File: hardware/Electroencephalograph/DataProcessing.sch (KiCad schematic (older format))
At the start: 20 parts, among them J3 Conn_01x04_Female, J4 Conn_01x04_Female, U3 STM32F030K6Tx, Y1 20MHz

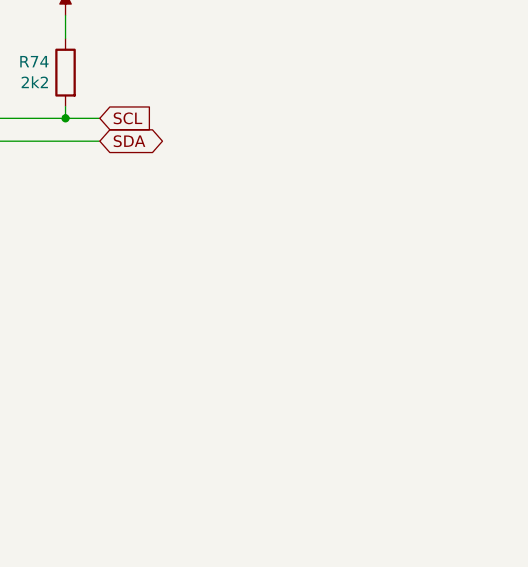
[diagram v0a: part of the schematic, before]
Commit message: split user interface to separate sheets
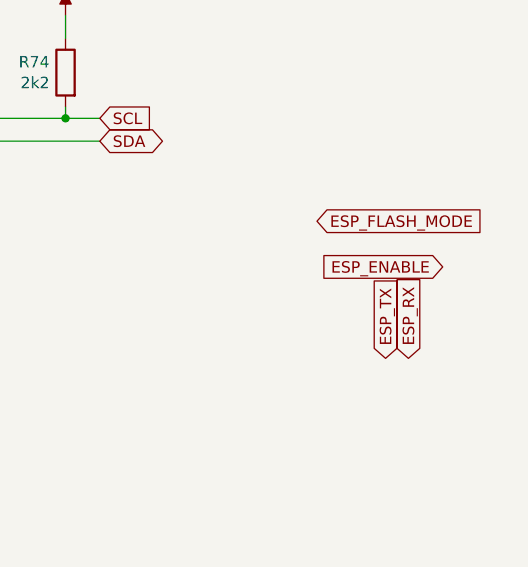
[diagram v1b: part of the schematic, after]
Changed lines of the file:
@@
 $Descr A4 11693 8268
 encoding utf-8
-Sheet 4 9
+Sheet 4 10
 Title "EEG signal processing"
 Date ""
@@
 Wire Wire Line
 	2400 3050 2400 3100
+Text GLabel 8100 4700 0    50   Input ~ 0
+ESP_ENABLE
+Text GLabel 7550 4500 2    50   Input ~ 0
+ESP_FLASH_MODE
+Text GLabel 7850 5100 1    50   Input ~ 0
+ESP_TX
+Text GLabel 7950 5100 1    50   Input ~ 0
+ESP_RX
 $EndSCHEMATC

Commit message: fix esp circuit
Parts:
- added R111, R112: 10R, Resistor_SMD:R_0402_1005Metric, symbol Device:R
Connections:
- net USART_RX: now also R111.1; no longer J4.3 (Pin_3)
- net USART_TX: now also R112.1; no longer J4.2 (Pin_2)
- new net: J4.2 (Pin_2), R112.2
- new net: J4.3 (Pin_3), R111.2
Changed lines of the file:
@@
 	1700 7200 1800 7200
 Wire Wire Line
-	1700 7000 1800 7000
-Wire Wire Line
-	1700 7100 1800 7100
-Text Label 1800 7100 0    50   ~ 0
+	2150 7000 2250 7000
+Wire Wire Line
+	2150 7100 2250 7100
+Text Label 2250 7100 0    50   ~ 0
 USART_TX
-Text Label 1800 7000 0    50   ~ 0
+Text Label 2250 7000 0    50   ~ 0
 USART_RX
 Wire Wire Line
@@
 Text GLabel 7950 5100 1    50   Input ~ 0
 ESP_RX
+Text GLabel 7500 4350 2    50   Input ~ 0
+CS_ESP
+$Comp
+L Device:R R?
+U 1 1 5F06BA33
+P 2000 7000
+AR Path="/5F06BA33" Ref="R?"  Part="1"
+AR Path="/5DAEEEF4/5F06BA33" Ref="R?"  Part="1"
+AR Path="/5DD5C7F6/5F06BA33" Ref="R?"  Part="1"
+AR Path="/5E142744/5F06BA33" Ref="R111"  Part="1"
+F 0 "R111" V 2207 7000 50  0000 C CNN
+F 1 "10R" V 2116 7000 50  0000 C CNN
+F 2 "Resistor_SMD:R_0402_1005Metric" V 1930 7000 50  0001 C CNN
+F 3 "~" H 2000 7000 50  0001 C CNN
+	1    2000 7000
+	0    1    -1   0
+$EndComp
+$Comp
+L Device:R R?
+U 1 1 5F06BF3F
+P 2000 7100
+AR Path="/5F06BF3F" Ref="R?"  Part="1"
+AR Path="/5DAEEEF4/5F06BF3F" Ref="R?"  Part="1"
+AR Path="/5DD5C7F6/5F06BF3F" Ref="R?"  Part="1"
+AR Path="/5E142744/5F06BF3F" Ref="R112"  Part="1"
+F 0 "R112" V 1885 7100 50  0000 C CNN
+F 1 "10R" V 1794 7100 50  0000 C CNN
+F 2 "Resistor_SMD:R_0402_1005Metric" V 1930 7100 50  0001 C CNN
+F 3 "~" H 2000 7100 50  0001 C CNN
+	1    2000 7100
+	0    1    -1   0
+$EndComp
+Wire Wire Line
+	1700 7000 1850 7000
+Wire Wire Line
+	1700 7100 1850 7100
 $EndSCHEMATC

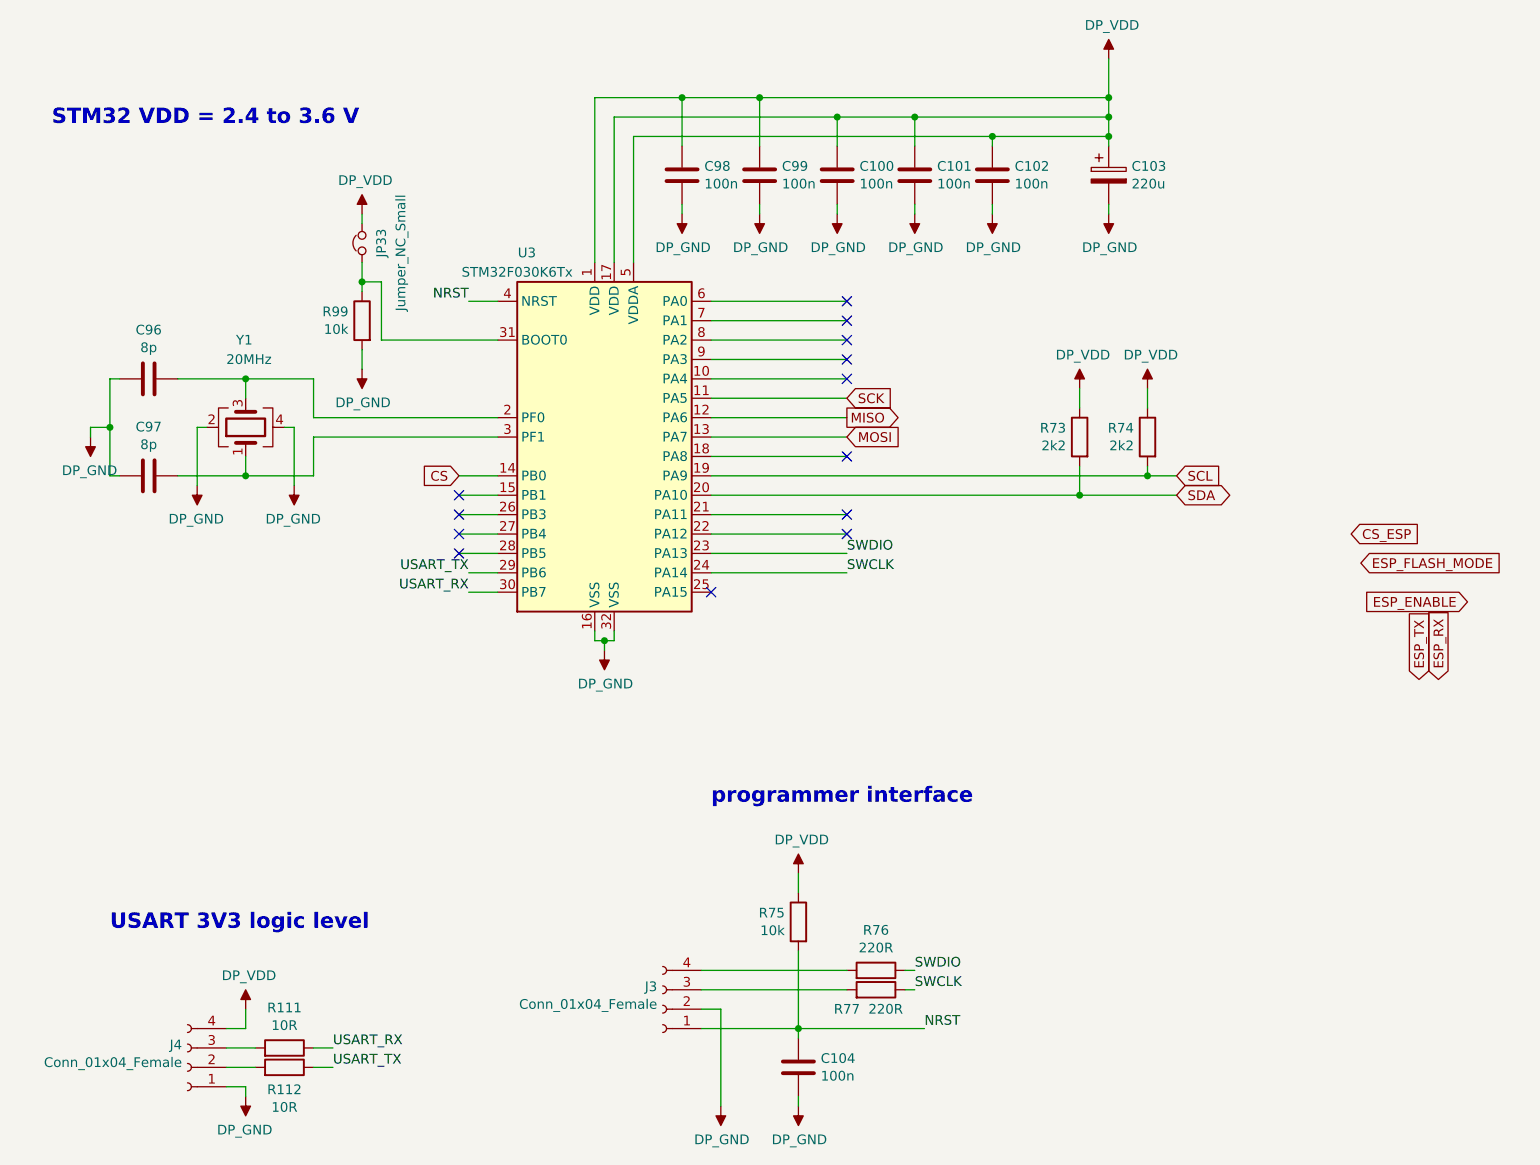
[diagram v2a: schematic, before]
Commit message: improve mcu component placement on pcb
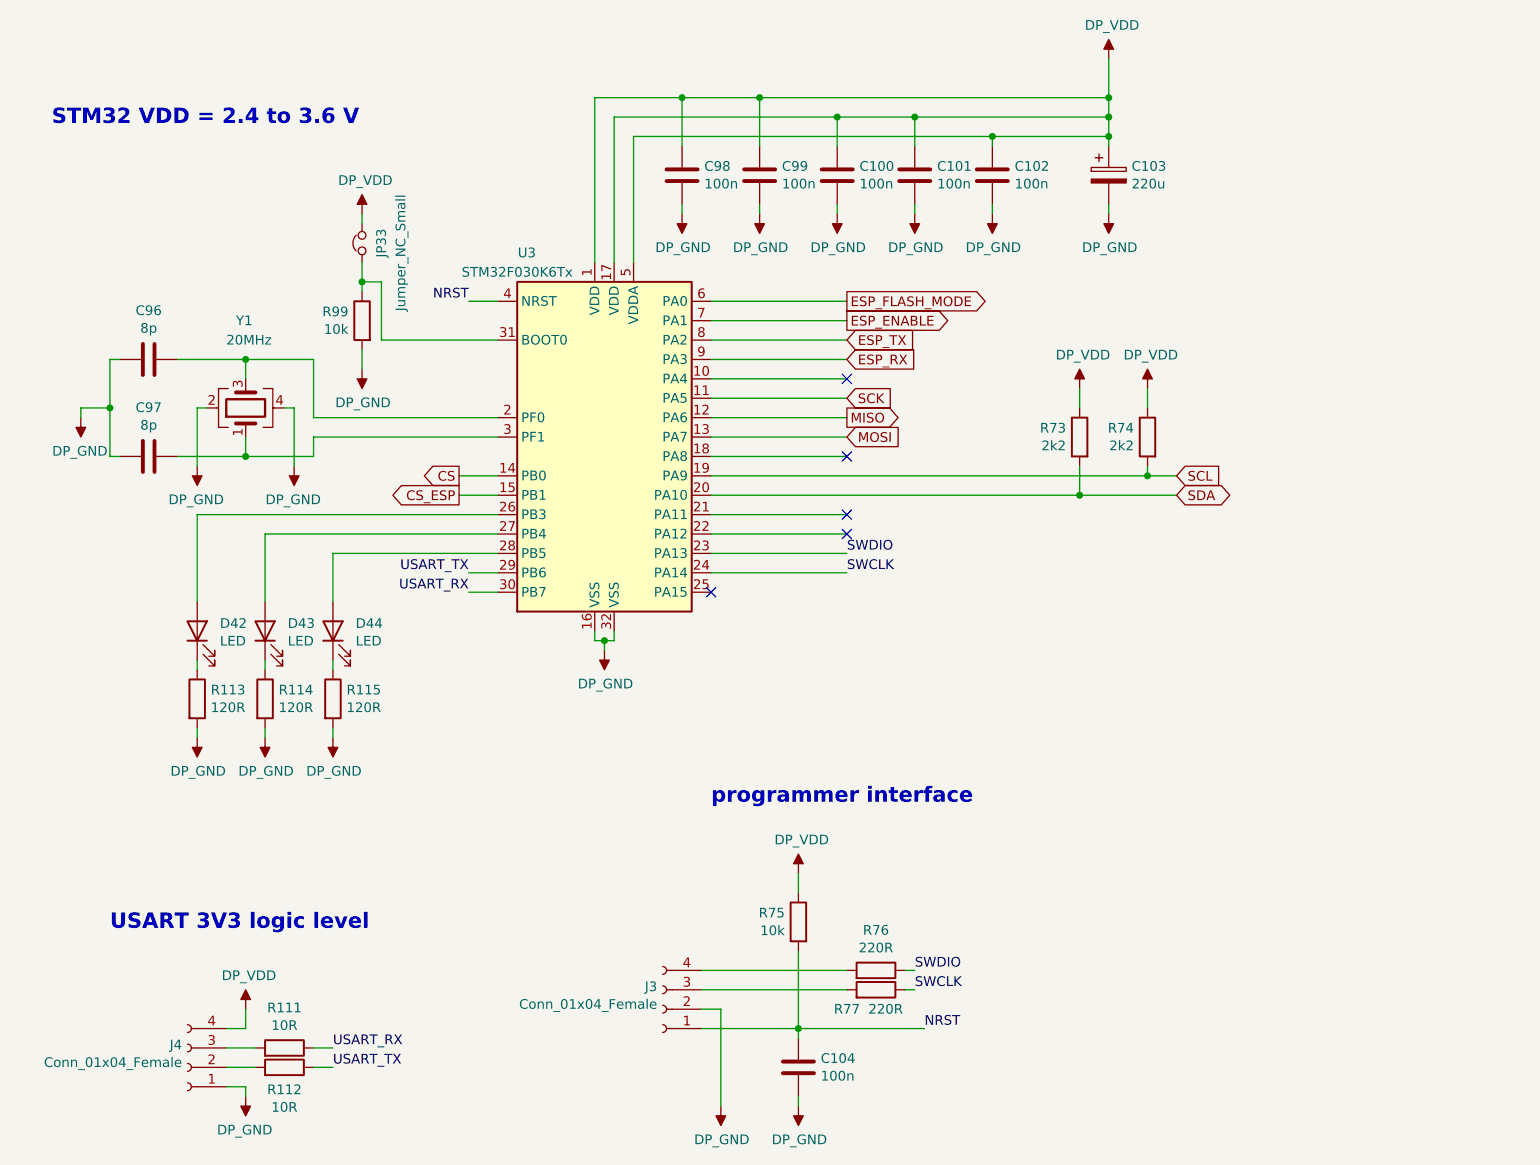
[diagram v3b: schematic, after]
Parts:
- added D42, D43, D44: LED, LED_SMD:LED_0402_1005Metric, symbol Device:LED
- added R113, R114, R115: 120R, Resistor_SMD:R_0402_1005Metric, symbol Device:R
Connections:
- net CS_ESP: now also U3.15 (PB1)
- net DP_GND: now also R113.2, R114.2, R115.2
- net ESP_ENABLE: now also U3.7 (PA1)
- net ESP_FLASH_MODE: now also U3.6 (PA0)
- net ESP_RX: now also U3.9 (PA3)
- net ESP_TX: now also U3.8 (PA2)
- net at U3.26 (PB3): now also D42.2 (A)
- net at U3.27 (PB4): now also D43.2 (A)
- net at U3.28 (PB5): now also D44.2 (A)
- new net: D42.1 (K), R113.1
- new net: D43.1 (K), R114.1
- new net: D44.1 (K), R115.1
- no-connect marks 13 -> 5
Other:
- moved on the sheet: C96, C97, Y1

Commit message: draft of mcu routing
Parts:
- added TP18, TP20, TP21, TP22, TP23, TP24, TP25, TP26, TP27, TP28: TestPoint, TestPoint:TestPoint_Pad_D1.0mm, symbol Connector:TestPoint
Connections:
- net CS_ESP: now also TP18.1
- net ESP_RX: now also TP21.1
- net ESP_TX: now also TP20.1
- net SCL: now also TP28.1
- net SDA: now also TP27.1
- net at U3.10 (PA4): now also TP22.1
- net at U3.18 (PA8): now also TP23.1
- net at U3.21 (PA11): now also TP24.1
- net at U3.22 (PA12): now also TP25.1
- net at U3.25 (PA15): now also TP26.1
- no-connect marks 5 -> 0
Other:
- moved on the sheet: R73, R74

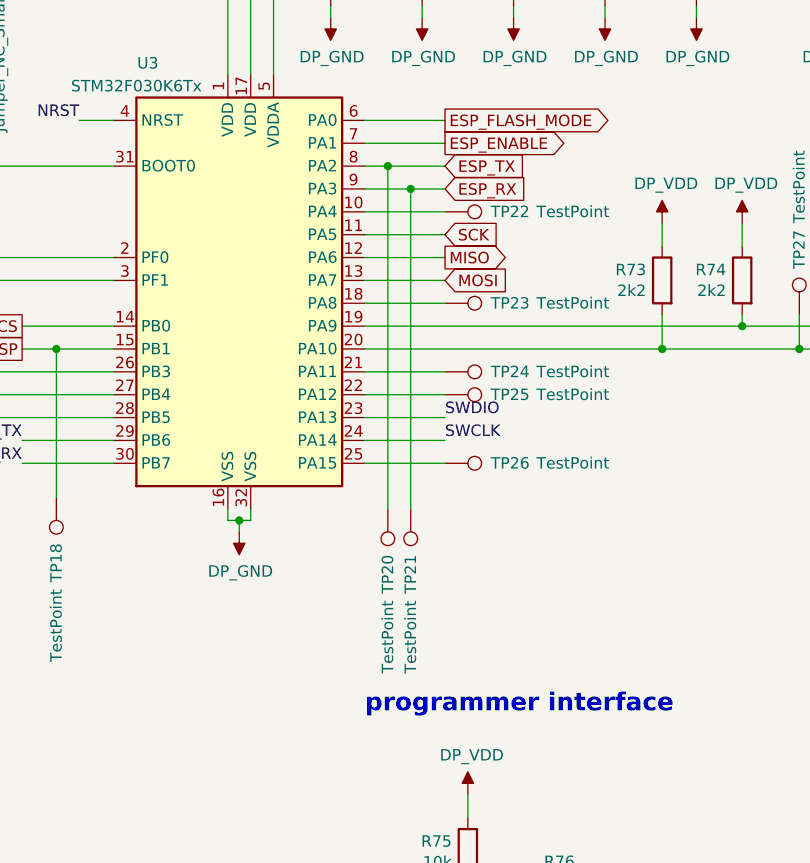
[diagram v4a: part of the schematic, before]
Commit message: further routing of cpu part
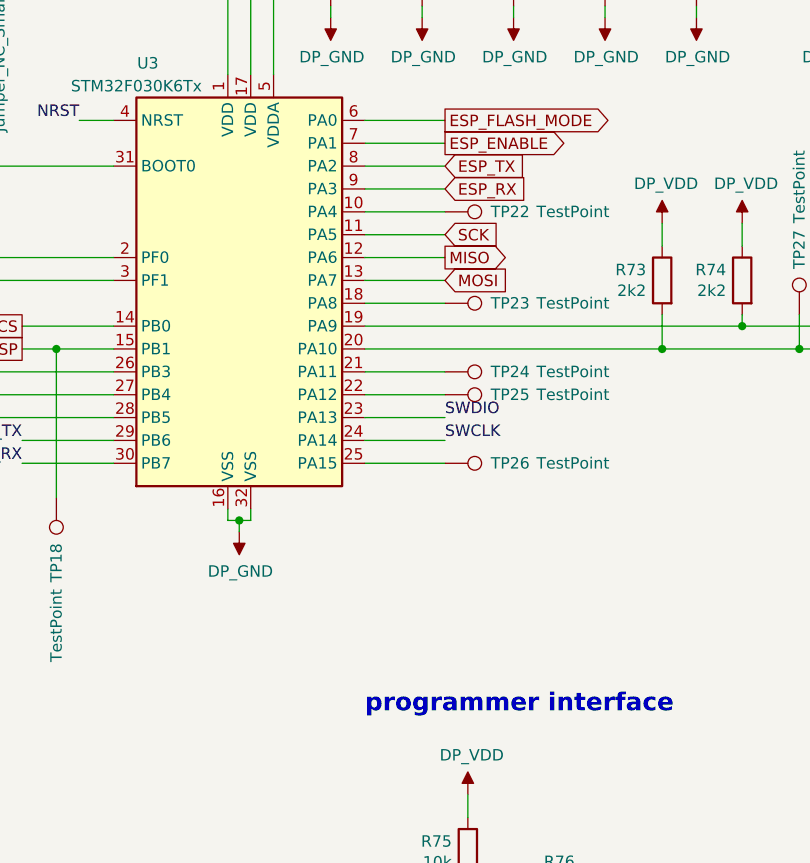
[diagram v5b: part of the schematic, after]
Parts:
- removed TP20, TP21: TestPoint, TestPoint:TestPoint_Pad_D1.0mm, symbol Connector:TestPoint
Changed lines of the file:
@@
 	4550 3550 4200 3550
-Wire Wire Line
-	4550 3450 4400 3450
 Wire Wire Line
 	4200 3850 4550 3850
@@
 Wire Wire Line
 	4550 3950 4200 3950
-Wire Wire Line
-	4200 3350 4300 3350
 Wire Wire Line
 	4200 4450 4550 4450
@@
 	0    1    1    0
 $EndComp
-$Comp
-L Connector:TestPoint TP20
-U 1 1 5F1139E2
-P 4300 4850
-F 0 "TP20" V 4300 5050 50  0000 L CNN
-F 1 "TestPoint" V 4300 5250 50  0000 L CNN
-F 2 "TestPoint:TestPoint_Pad_D1.0mm" H 4500 4850 50  0001 C CNN
-F 3 "~" H 4500 4850 50  0001 C CNN
-	1    4300 4850
-	-1   0    0    1
-$EndComp
 Wire Wire Line
 	4200 4650 4550 4650
-$Comp
-L Connector:TestPoint TP21
-U 1 1 5F11CFF6
-P 4400 4850
-F 0 "TP21" V 4400 5050 50  0000 L CNN
-F 1 "TestPoint" V 4400 5250 50  0000 L CNN
-F 2 "TestPoint:TestPoint_Pad_D1.0mm" H 4600 4850 50  0001 C CNN
-F 3 "~" H 4600 4850 50  0001 C CNN
-	1    4400 4850
-	-1   0    0    1
-$EndComp
-Wire Wire Line
-	4300 4850 4300 3350
-Connection ~ 4300 3350
-Wire Wire Line
-	4300 3350 4550 3350
-Wire Wire Line
-	4400 4850 4400 3450
-Connection ~ 4400 3450
-Wire Wire Line
-	4400 3450 4200 3450
 $Comp
 L Connector:TestPoint TP28
@@
 Wire Wire Line
 	2700 4050 3100 4050
+Wire Wire Line
+	4200 3350 4550 3350
+Wire Wire Line
+	4200 3450 4550 3450
 $EndSCHEMATC
